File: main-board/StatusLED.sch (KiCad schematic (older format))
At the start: 0 parts

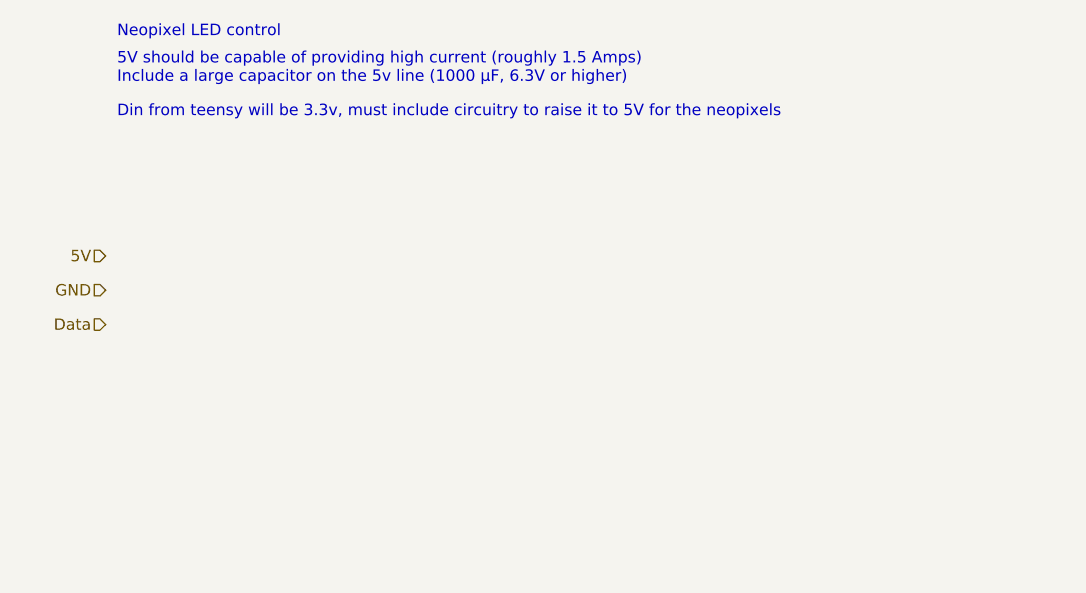
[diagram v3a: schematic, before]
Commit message: More subsheets
Added gps and LED ring
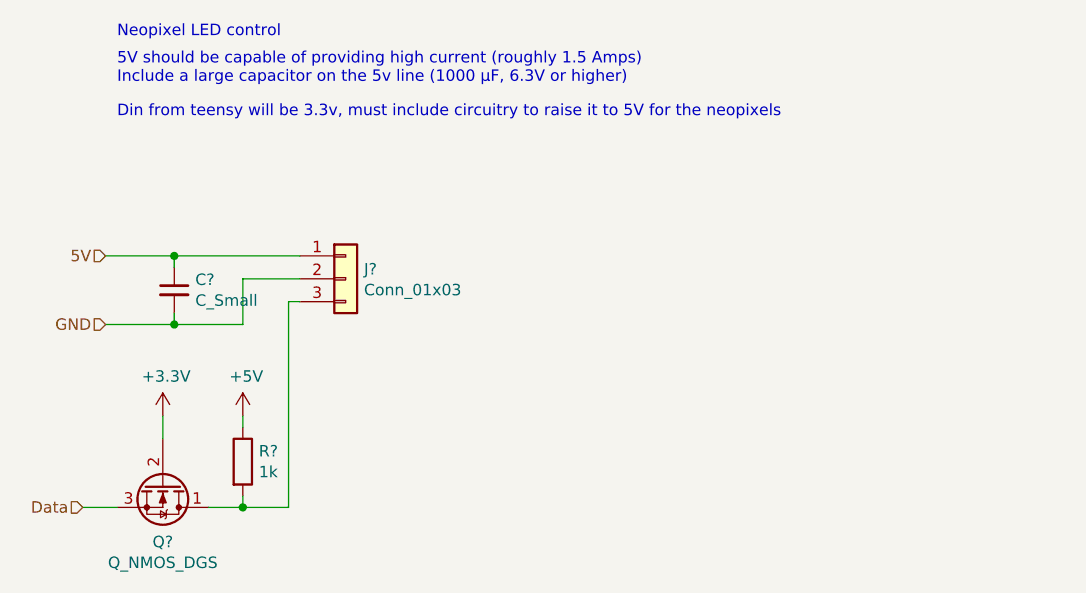
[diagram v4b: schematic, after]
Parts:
- added C?: C_Small, symbol Device:C_Small
- added J?: Conn_01x03, symbol Connector_Generic:Conn_01x03
- added Q?: Q_NMOS_DGS, symbol Device:Q_NMOS_DGS
- added R?: 1k, symbol Device:R
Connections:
- net 5V: now also C?.1, J?.1 (Pin_1)
- net Data: now also Q?.3 (S)
- net GND: now also C?.2, J?.2 (Pin_2)
- new net: J?.3 (Pin_3), Q?.1 (D), R?.2
- new net +3V3: Q?.2 (G)
- new net +5V: R?.1
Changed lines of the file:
@@
 Text HLabel 5200 2700 0    50   Input ~ 0
 5V
-Text HLabel 5200 2850 0    50   Input ~ 0
+Text HLabel 5200 3000 0    50   Input ~ 0
 GND
-Text HLabel 5200 3000 0    50   Input ~ 0
+Text HLabel 5100 3800 0    50   Input ~ 0
 Data
 Text Notes 5250 1750 0    50   ~ 0
@@
 Text Notes 5250 2100 0    50   ~ 0
 Din from teensy will be 3.3v, must include circuitry to raise it to 5V for the neopixels
+$Comp
+L Device:C_Small C?
+U 1 1 60AFFE8F
+P 5500 2850
+F 0 "C?" H 5592 2896 50  0000 L CNN
+F 1 "C_Small" H 5592 2805 50  0000 L CNN
+F 2 "" H 5500 2850 50  0001 C CNN
+F 3 "~" H 5500 2850 50  0001 C CNN
+	1    5500 2850
+	1    0    0    -1
+$EndComp
+Wire Wire Line
+	5200 2700 5500 2700
+Wire Wire Line
+	5500 2700 5500 2750
+Wire Wire Line
+	5500 2950 5500 3000
+Wire Wire Line
+	5500 3000 5200 3000
+$Comp
+L Connector_Generic:Conn_01x03 J?
+U 1 1 60B011A5
+P 6250 2800
+F 0 "J?" H 6330 2842 50  0000 L CNN
+F 1 "Conn_01x03" H 6330 2751 50  0000 L CNN
+F 2 "" H 6250 2800 50  0001 C CNN
+F 3 "~" H 6250 2800 50  0001 C CNN
+	1    6250 2800
+	1    0    0    -1
+$EndComp
+Wire Wire Line
+	6050 2700 5500 2700
+Connection ~ 5500 2700
+Wire Wire Line
+	6050 2800 5800 2800
+Wire Wire Line
+	5800 2800 5800 3000
+Wire Wire Line
+	5800 3000 5500 3000
+Connection ~ 5500 3000
+Wire Wire Line
+	6050 2900 6000 2900
+Wire Wire Line
+	5250 3800 5100 3800
+Wire Wire Line
+	6000 2900 6000 3800
+Wire Wire Line
+	5800 3400 5800 3450
+$Comp
+L power:+5V #PWR?
+U 1 1 60B006D4
+P 5800 3400
+F 0 "#PWR?" H 5800 3250 50  0001 C CNN
+F 1 "+5V" H 5815 3573 50  0000 C CNN
+F 2 "" H 5800 3400 50  0001 C CNN
+F 3 "" H 5800 3400 50  0001 C CNN
+	1    5800 3400
+	1    0    0    -1
+$EndComp
+Wire Wire Line
+	5800 3750 5800 3800
+Wire Wire Line
+	5800 3800 5650 3800
+Connection ~ 5800 3800
+Wire Wire Line
+	6000 3800 5800 3800
+$Comp
+L Device:R R?
+U 1 1 60AFF563
+P 5800 3600
+F 0 "R?" H 5870 3646 50  0000 L CNN
+F 1 "1k" H 5870 3555 50  0000 L CNN
+F 2 "" V 5730 3600 50  0001 C CNN
+F 3 "~" H 5800 3600 50  0001 C CNN
+	1    5800 3600
+	1    0    0    -1
+$EndComp
+Wire Wire Line
+	5450 3400 5450 3500
+$Comp
+L power:+3.3V #PWR?
+U 1 1 60B01172
+P 5450 3400
+F 0 "#PWR?" H 5450 3250 50  0001 C CNN
+F 1 "+3.3V" H 5465 3573 50  0000 C CNN
+F 2 "" H 5450 3400 50  0001 C CNN
+F 3 "" H 5450 3400 50  0001 C CNN
+	1    5450 3400
+	1    0    0    -1
+$EndComp
+$Comp
+L Device:Q_NMOS_DGS Q?
+U 1 1 60AFD36F
+P 5450 3700
+F 0 "Q?" V 5701 3700 50  0000 C CNN
+F 1 "Q_NMOS_DGS" V 5792 3700 50  0000 C CNN
+F 2 "" H 5650 3800 50  0001 C CNN
+F 3 "~" H 5450 3700 50  0001 C CNN
+	1    5450 3700
+	0    1    1    0
+$EndComp
 $EndSCHEMATC
